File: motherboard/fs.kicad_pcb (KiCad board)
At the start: 4 copper layers, 177.8 x 114.3 mm, 265 parts, among them J101 Header, J102 640389-2, J103 Conn_01x05, J201 BNC, J203 BNC, J301 BNC, J302 BNC, J303 BNC, J304 BNC, J305 BNC, J306 BNC, Q101 MJD44H11, Q102 MJD45H11, Q103 2N7002, Q203 2N7002, U101 INA132UA, U102 LM741C, U103 LMH6609, U104 LM317, U105 LM337, U106 LM340-5, U107 MC7905ACD2T, U108 DG419DY, U201 LMH6609, U202 SYPD-1, U203 LM393, U204 AD797AR, U205 LM393, U206 OPA192IDR, U207 DG419DY, U301 LMH6609, U302 LMH6609, U303 LMH6609, U304 LMH6609, U305 LMH6609, U306 LMH6609

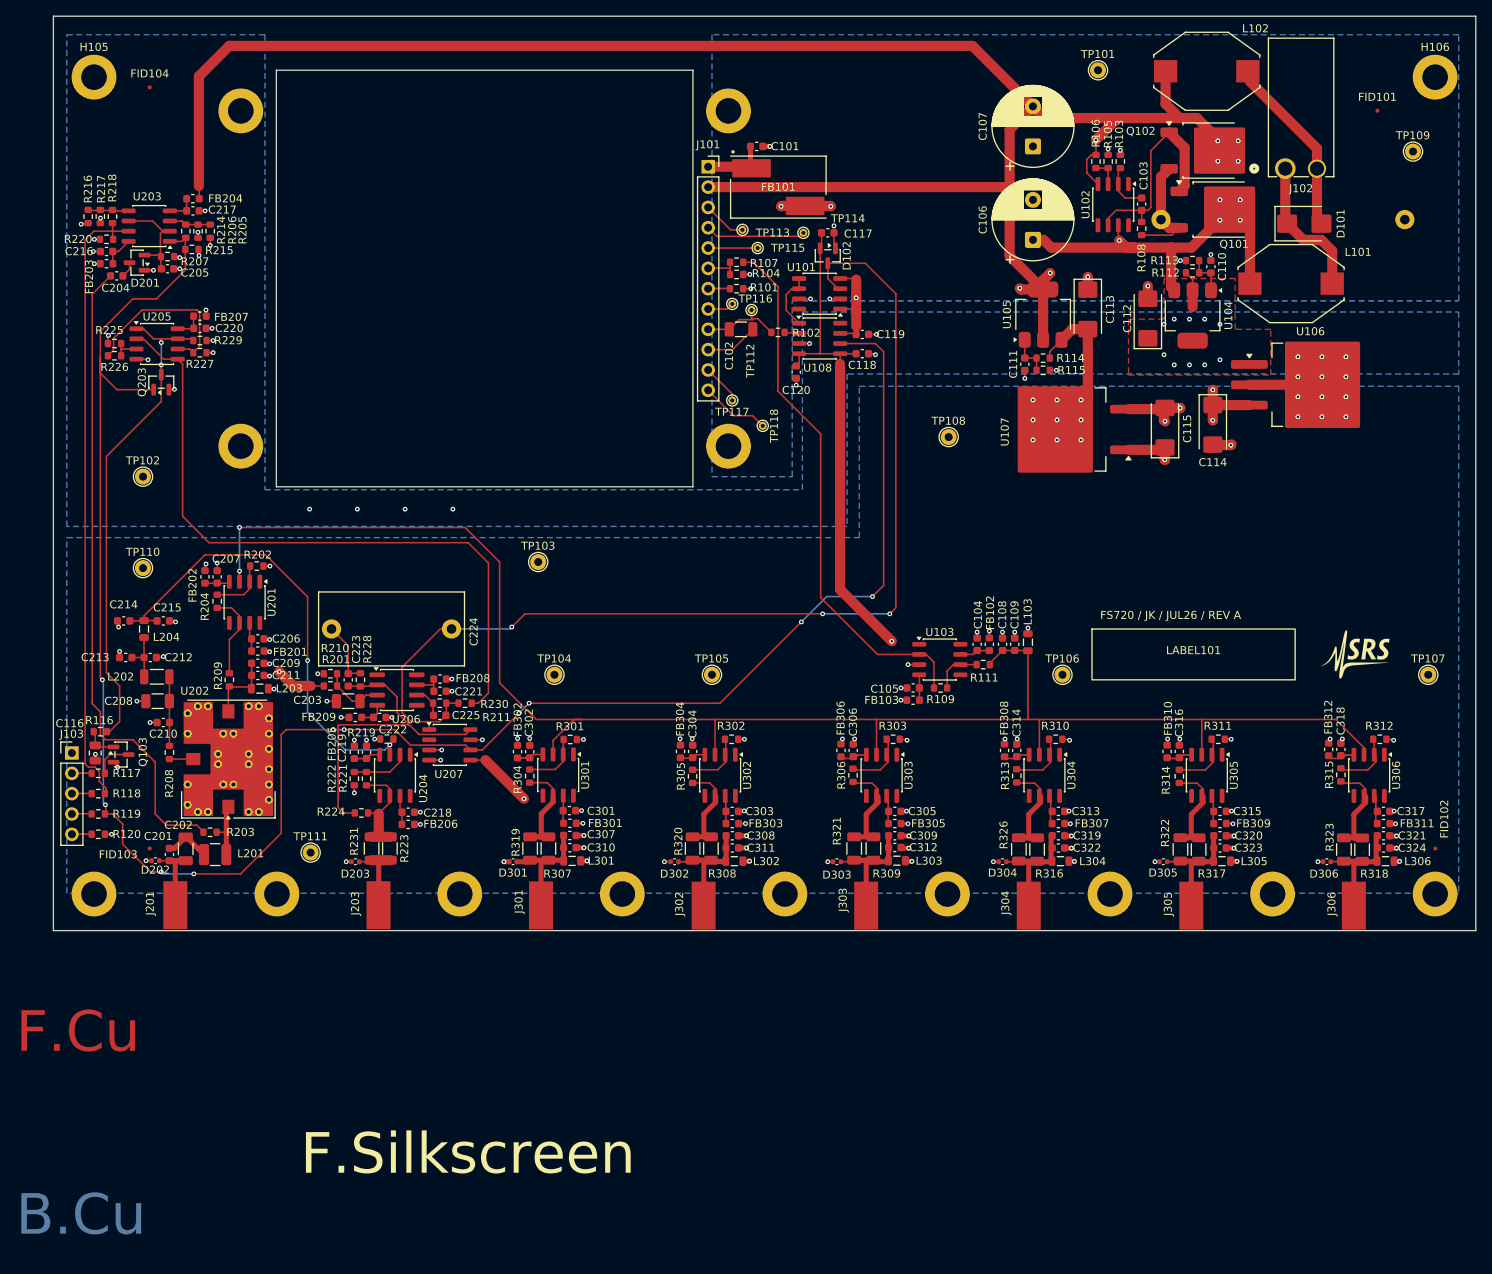
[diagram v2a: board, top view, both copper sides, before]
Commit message: better comparators for ~FAULT
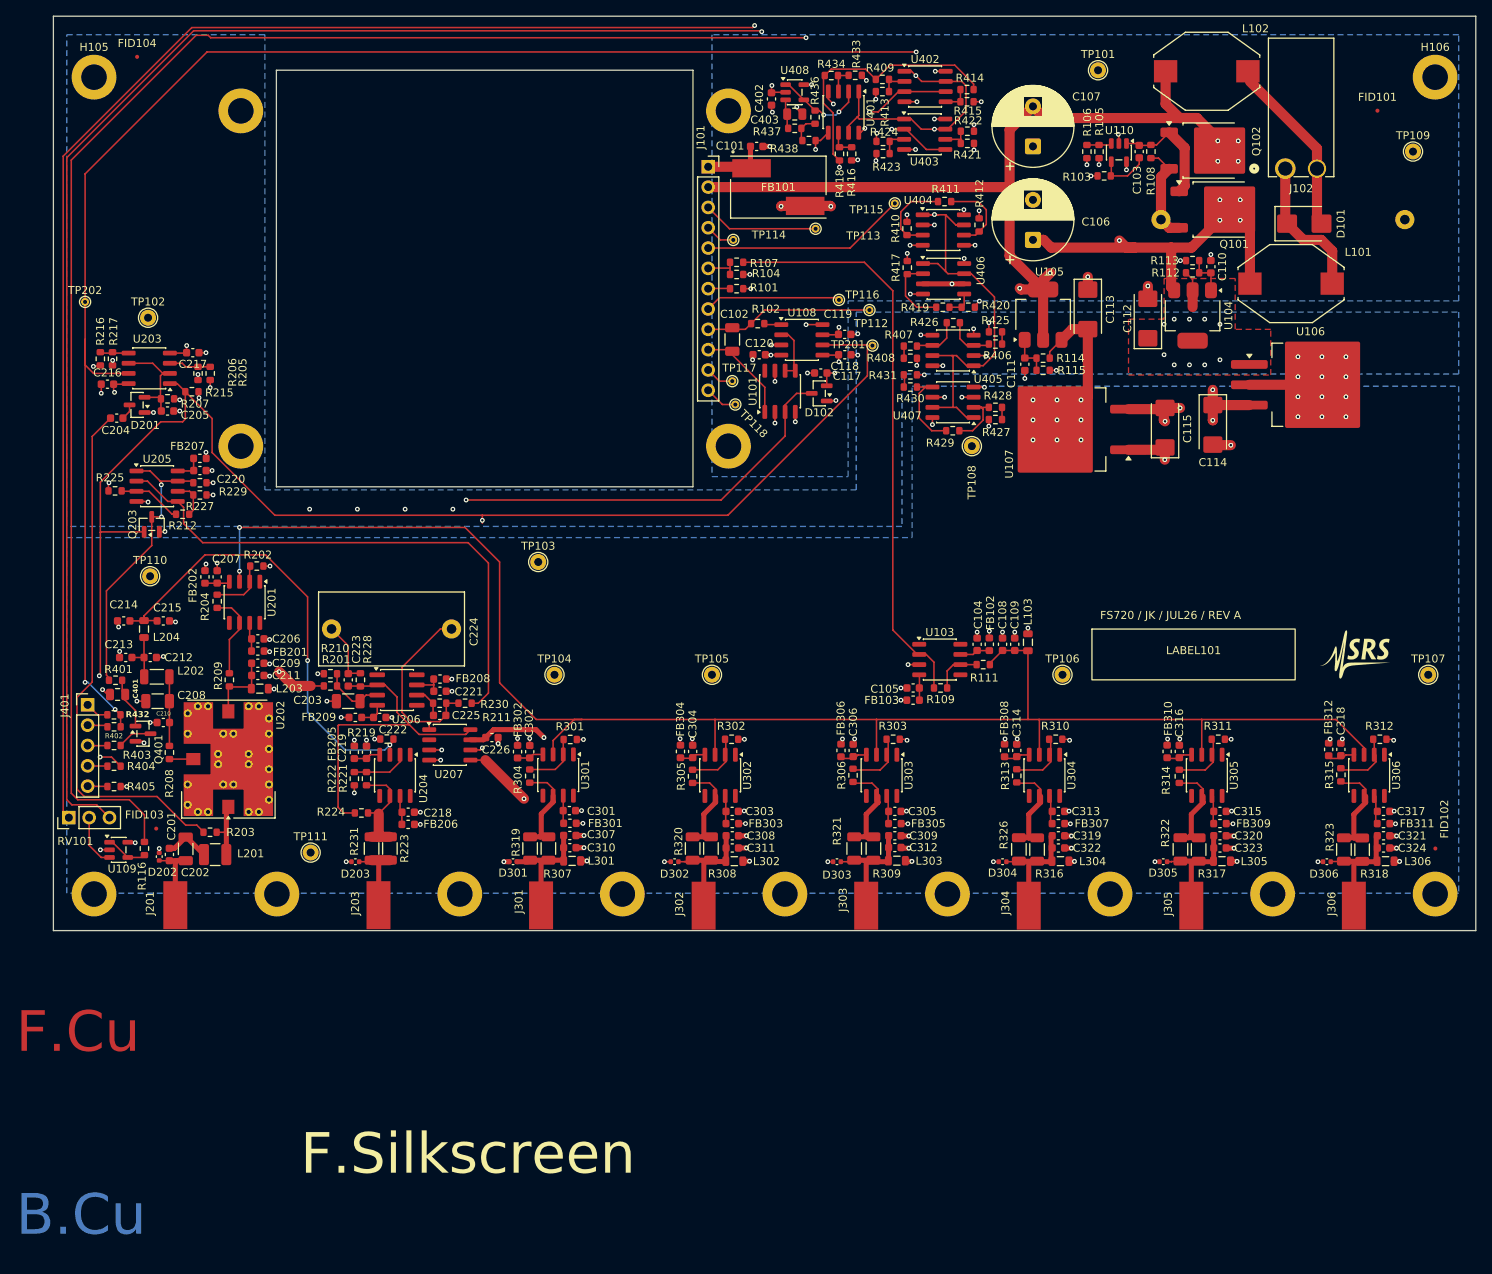
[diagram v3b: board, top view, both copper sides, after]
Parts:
- removed C116: 10μF, Capacitor_SMD:C_0805_2012Metric
- removed FB203, FB204: 742863160, Inductor_SMD:L_0603_1608Metric
- removed J103: Conn_01x05, Connector_PinHeader_2.54mm:PinHeader_1x05_P2.54mm_Vertical
- removed Q103: 2N7002, Package_TO_SOT_SMD:SOT-23
- removed R117, R120: 1.00K, Resistor_SMD:R_0603_1608Metric
- removed R118, R119: 4.99K, Resistor_SMD:R_0603_1608Metric
- removed R214: 43.2K, Resistor_SMD:R_0603_1608Metric
- removed R218: 1.00M, Resistor_SMD:R_0603_1608Metric
- removed R220: 10.0K, Resistor_SMD:R_0603_1608Metric
- removed R226: 8.06K, Resistor_SMD:R_0603_1608Metric
- removed U102: LM741C, Package_SO:SO-8_3.9x4.9mm_P1.27mm
- added C226: 0.1μF, Capacitor_SMD:C_0603_1608Metric, F.Cu at (87.4, 120.2)
- added C401: 10μF, Capacitor_SMD:C_0805_2012Metric, F.Cu at (40.6, 114.9)
- added C402: 0.1μF, Capacitor_SMD:C_0603_1608Metric, F.Cu at (122.4, 40.4)
- added C403: 10μF, Capacitor_SMD:C_0805_2012Metric, F.Cu at (125.3, 42.3)
- added J401: Conn_01x05, Connector_PinHeader_2.54mm:PinHeader_1x05_P2.54mm_Vertical, F.Cu at (36.9, 116.2)
- added Q401: 2N7002, Package_TO_SOT_SMD:SOT-23, F.Cu at (43.8, 119.8)
- added R212: 10.0K, Resistor_SMD:R_0603_1608Metric, F.Cu at (48.8, 92.3)
- added R401: 10.0K, Resistor_SMD:R_0603_1608Metric, F.Cu at (40.4, 113.1)
- added R402: 1.00K, Resistor_SMD:R_0603_1608Metric, F.Cu at (40.2, 118.9)
- added R403: 4.99K, Resistor_SMD:R_0603_1608Metric, F.Cu at (40.2, 121.2)
- added R404: 4.99K, Resistor_SMD:R_0603_1608Metric, F.Cu at (40.2, 123.8)
- added R405: 1.00K, Resistor_SMD:R_0603_1608Metric, F.Cu at (40.2, 126.4)
- added R406: 4.99K, Resistor_SMD:R_0603_1608Metric, F.Cu at (150.4, 71.1)
- added R407: 10.0K, Resistor_SMD:R_0603_1608Metric, F.Cu at (139.7, 71.3)
- added R408: 10.0K, Resistor_SMD:R_0603_1608Metric, F.Cu at (139.7, 72.8)
- added R409: 100K, Resistor_SMD:R_0603_1608Metric, F.Cu at (136.2, 38.0)
- added R410: 43.2K, Resistor_SMD:R_0603_1608Metric, F.Cu at (139.3, 56.6)
- added R411: 4.99K, Resistor_SMD:R_0603_1608Metric, F.Cu at (144.0, 53.2)
- added R412: 30.1K, Resistor_SMD:R_0603_1608Metric, F.Cu at (148.3, 56.2)
- added R413: 10.0K, Resistor_SMD:R_0603_1608Metric, F.Cu at (136.2, 39.5)
- added R414: 10.0K, Resistor_SMD:R_0603_1608Metric, F.Cu at (146.8, 39.2)
- added R415: 100K, Resistor_SMD:R_0603_1608Metric, F.Cu at (146.8, 40.8)
- added R416: 100R, Resistor_SMD:R_0603_1608Metric, F.Cu at (132.4, 47.3)
- added R417: 43.2K, Resistor_SMD:R_0603_1608Metric, F.Cu at (139.4, 61.5)
- added R418: 4.99K, Resistor_SMD:R_0603_1608Metric, F.Cu at (130.9, 47.3)
- added R419: 4.99K, Resistor_SMD:R_0603_1608Metric, F.Cu at (143.8, 66.5)
- added R420: 30.1K, Resistor_SMD:R_0603_1608Metric, F.Cu at (147.0, 66.5)
- added R421: 10.0K, Resistor_SMD:R_0603_1608Metric, F.Cu at (146.9, 46.0)
- added R422: 1.00K, Resistor_SMD:R_0603_1608Metric, F.Cu at (146.9, 44.5)
- added R423: 4.99K, Resistor_SMD:R_0603_1608Metric, F.Cu at (136.3, 47.2)
- added R424: 1.00K, Resistor_SMD:R_0603_1608Metric, F.Cu at (136.3, 45.7)
- added R425: 10.0K, Resistor_SMD:R_0603_1608Metric, F.Cu at (150.4, 69.5)
- added R426: 4.99K, Resistor_SMD:R_0603_1608Metric, F.Cu at (145.1, 68.4)
- added R427: 10.0K, Resistor_SMD:R_0603_1608Metric, F.Cu at (150.4, 80.5)
- added R428: 4.99K, Resistor_SMD:R_0603_1608Metric, F.Cu at (150.4, 79.0)
- added R429: 4.99K, Resistor_SMD:R_0603_1608Metric, F.Cu at (145.0, 81.9)
- added R430: 10.0K, Resistor_SMD:R_0603_1608Metric, F.Cu at (139.7, 76.4)
- added R431: 10.0K, Resistor_SMD:R_0603_1608Metric, F.Cu at (139.7, 74.9)
- added R432: 10.0K, Resistor_SMD:R_0603_1608Metric, F.Cu at (40.2, 117.4)
- added R433: 43.2K, Resistor_SMD:R_0603_1608Metric, F.Cu at (132.8, 37.5)
- added R434: 10.0K, Resistor_SMD:R_0603_1608Metric, F.Cu at (129.9, 37.5)
- added R436: 30.1K, Resistor_SMD:R_0603_1608Metric, F.Cu at (127.8, 42.7)
- added R437: 1.00M, Resistor_SMD:R_0603_1608Metric, F.Cu at (125.3, 44.1)
- added R438: 1.00M, Resistor_SMD:R_0603_1608Metric, F.Cu at (127.1, 45.6)
- added RV101: 10k, Connector_PinHeader_2.54mm:PinHeader_1x03_P2.54mm_Vertical, F.Cu at (34.5, 130.3)
- added TP201: TestPoint, TestPoint:TestPoint_THTPad_D1.0mm_Drill0.5mm, F.Cu at (135.0, 71.2)
- added TP202: TestPoint, TestPoint:TestPoint_THTPad_D1.0mm_Drill0.5mm, F.Cu at (36.6, 65.8)
- added U109: NCS20071, Package_TO_SOT_SMD:TSOT-23-5, F.Cu at (40.8, 134.3)
- added U110: NCS20071, Package_TO_SOT_SMD:TSOT-23-5, F.Cu at (165.8, 47.1)
- added U401: LM393, Package_SO:SO-8_3.9x4.9mm_P1.27mm, F.Cu at (131.4, 42.1)
- added U402: LM393, Package_SO:SO-8_3.9x4.9mm_P1.27mm, F.Cu at (141.6, 38.9)
- added U403: LM393, Package_SO:SO-8_3.9x4.9mm_P1.27mm, F.Cu at (141.5, 44.8)
- added U404: LM393, Package_SO:SO-8_3.9x4.9mm_P1.27mm, F.Cu at (143.9, 56.8)
- added U405: LM393, Package_SO:SO-8_3.9x4.9mm_P1.27mm, F.Cu at (145.1, 71.9)
- added U406: LM393, Package_SO:SO-8_3.9x4.9mm_P1.27mm, F.Cu at (143.9, 62.9)
- added U407: LM393, Package_SO:SO-8_3.9x4.9mm_P1.27mm, F.Cu at (145.1, 78.3)
- added U408: NCS20071, Package_TO_SOT_SMD:TSOT-23-5, F.Cu at (125.3, 39.6)
- D101: value MMBD352LT1G -> MBRS230LT3G
- D102, D201: value MMBD352 -> MMBD352LT1G
- R102: value 1.00K -> 100R
- R116: value 10.0K -> 1.00K
- moved TP102 19.9 mm to (44.5, 67.8)
- moved R225 18.4 mm to (40.3, 89.4)
- moved TP115 18.0 mm to (137.8, 53.5)
- moved R216 17.8 mm to (38.5, 72.9)
- moved R217 17.8 mm to (40.0, 72.9)
- moved Q203 17.8 mm to (44.9, 93.6)
- moved C205 17.8 mm to (46.9, 79.4)
- moved C220 17.8 mm to (50.9, 86.9)
- moved D201 17.8 mm to (43.1, 78.7)
- moved FB207 17.8 mm to (50.9, 85.3)
- moved R205 17.8 mm to (52.2, 74.7)
- moved R206 17.8 mm to (50.7, 74.7)
- moved R207 17.8 mm to (46.9, 77.9)
- moved R215 17.8 mm to (49.9, 77.0)
- moved R227 17.8 mm to (50.9, 89.9)
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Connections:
- net Net-(C204-Pad1) renamed /Phase Noise/REF_IN_MON
- C216 pad 2: Net-(U203C-V+) -> +9V
- C217 pad 2: Net-(U203C-V-) -> -12V
- Q203 pad 3: /LOCKED -> /~{LOCKED}
- R116 pad 1: /LOCKED -> Net-(U109--)
- R116 pad 2: Net-(Q103-G) -> Net-(R116-Pad2)
- R229 pad 1: /LOCKED -> /~{LOCKED}
- U108 pad 1: Net-(U101-SENSE) -> Net-(R102-Pad2)
- U108 pad 2: Net-(R102-Pad2) -> Net-(U101-SENSE)
- U108 pad 8: unconnected-(U108-Pad8) -> Net-(R116-Pad2)
- U203 pad 4: Net-(U203C-V-) -> -12V
- U203 pad 7: /~{OVLD} -> /~{FAULT}
- U203 pad 8: Net-(U203C-V+) -> +9V
- U205 pad 1: /LOCKED -> /~{LOCKED}
- U205 pad 7: /LOCKED -> /~{LOCKED}
- U207 pad 7: -9V -> -12V
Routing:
- net /~{FAULT}: track 0.00 -> 288.9 mm, vias 0 -> 6
- net /SC10L_+5VREF: track 3.28 -> 280.4 mm, vias 0 -> 2
- net Net-(R116-Pad2): track 0.00 -> 229.2 mm, vias 0 -> 2
- net -12V: track 264.8 -> 392.5 mm, vias 8 -> 30
- net /~{OVLD}: track 78.7 -> 0.00 mm
- net /LOCKED: track 61.2 -> 0.00 mm, vias 2 -> 0
- net +5V: track 96.3 -> 48.9 mm, vias 17 -> 22
- net /~{SIG_PRESENT}: track 251.3 -> 205.3 mm, vias 10 -> 4
- net /SC10L_FREQ_CTL: track 10.5 -> 55.7 mm, vias 0 -> 1
- net /Phase Noise/FREQ_CTL: track 134.2 -> 92.0 mm, vias 3 -> 1
- net /AGC_MON: track 6.19 -> 42.6 mm, vias 0 -> 1
- net /~{LOCKED}: track 0.00 -> 35.8 mm, vias 0 -> 2
- net +12V: track 54.0 -> 86.4 mm, vias 8 -> 17
- net -5V: track 14.7 -> 40.8 mm, vias 10 -> 13
- net /HEAT_MON: track 5.44 -> 27.6 mm, vias 0 -> 1
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- added copper zone on In3.Cu, net +5V
- added copper zone on In2.Cu, net -12V
- removed copper zone on In2.Cu, net +5V
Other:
- copper layers 4 -> 6

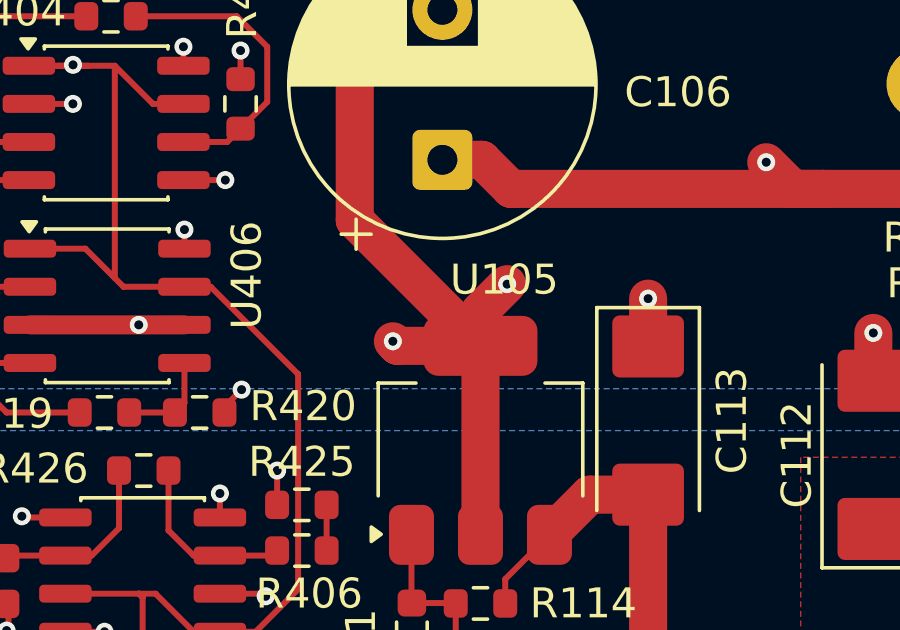
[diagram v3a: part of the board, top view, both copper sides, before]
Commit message: fix net directions
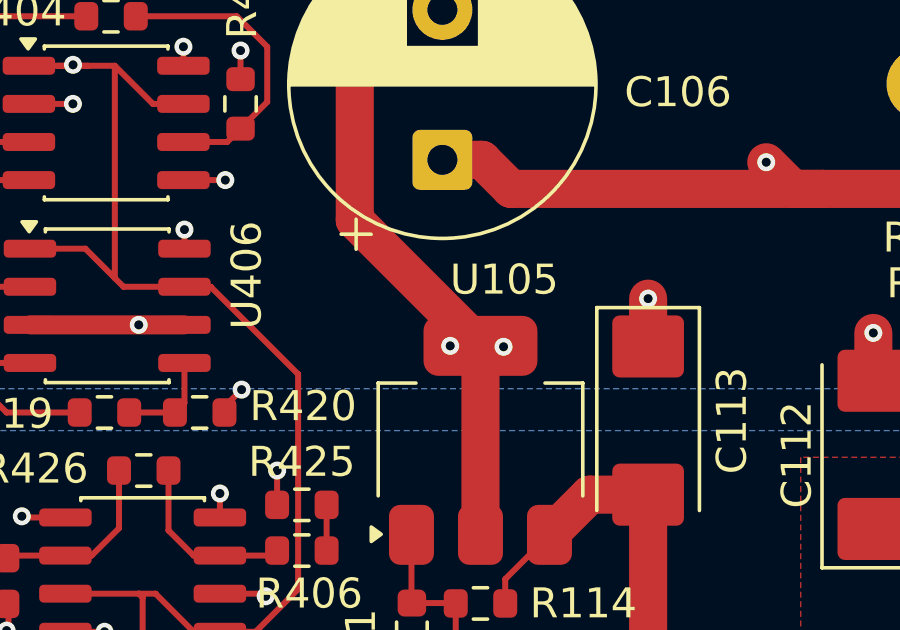
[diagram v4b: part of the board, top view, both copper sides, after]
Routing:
- net -12V: track 392.5 -> 388.1 mm
